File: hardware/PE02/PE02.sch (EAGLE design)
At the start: 23 parts, among them IC1 MSP430G2231, IC2 TPS78233

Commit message: Fixed buzzer, need to alter package of GND sewtab to make pad for vibration sensor
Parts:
- added JP1: (no value), adafruit:PINHD-1X1CB
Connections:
- net BUZZ: now also JP1.1
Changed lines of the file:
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@@
 <part name="TP1" library="adafruit" deviceset="SEWTAP" device="0.4IN"/>
 <part name="TP2" library="adafruit" deviceset="SEWTAP" device="0.4IN"/>
+<part name="JP1" library="adafruit" deviceset="PINHD-1X1" device="CB"/>
 </parts>
 <sheets>
@@
 <instance part="TP1" gate="G$1" x="-30.48" y="50.8" rot="R180"/>
 <instance part="TP2" gate="G$1" x="-30.48" y="35.56" rot="R180"/>
+<instance part="JP1" gate="G$1" x="86.36" y="73.66" rot="R270"/>
 </instances>
 <busses>
@@
 <segment>
 <pinref part="IC1" gate="G$1" pin="12"/>
-<wire x1="68.58" y1="60.96" x2="76.2" y2="60.96" width="0.1524" layer="91"/>
 <label x="71.12" y="60.96" size="1.778" layer="95"/>
-</segment>
-</net>
+<wire x1="86.36" y1="60.96" x2="68.58" y2="60.96" width="0.1524" layer="91"/>
+<pinref part="JP1" gate="G$1" pin="1"/>
+<wire x1="86.36" y1="60.96" x2="86.36" y2="76.2" width="0.1524" layer="91"/>
+</segment>
+</net>

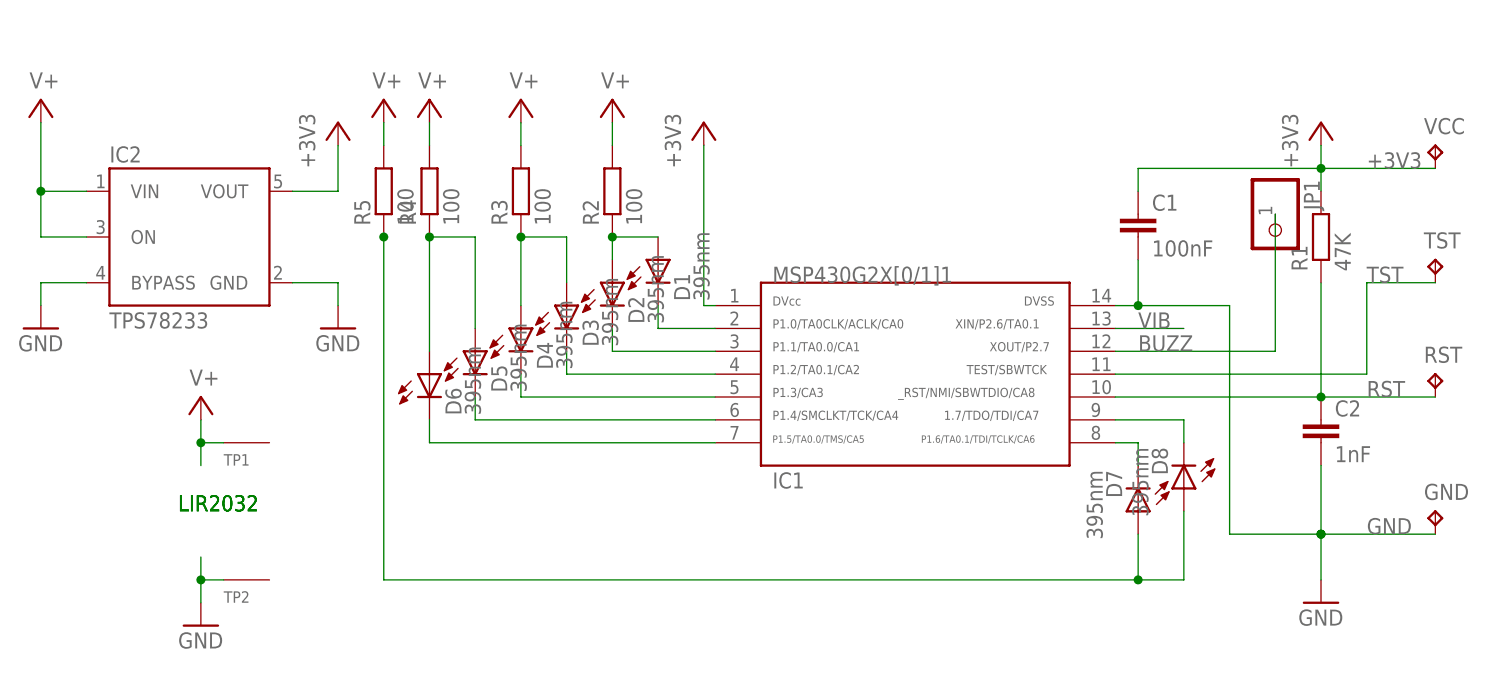
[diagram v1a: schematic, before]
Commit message: 2.2V supply, pullup vibration sensor to output pin
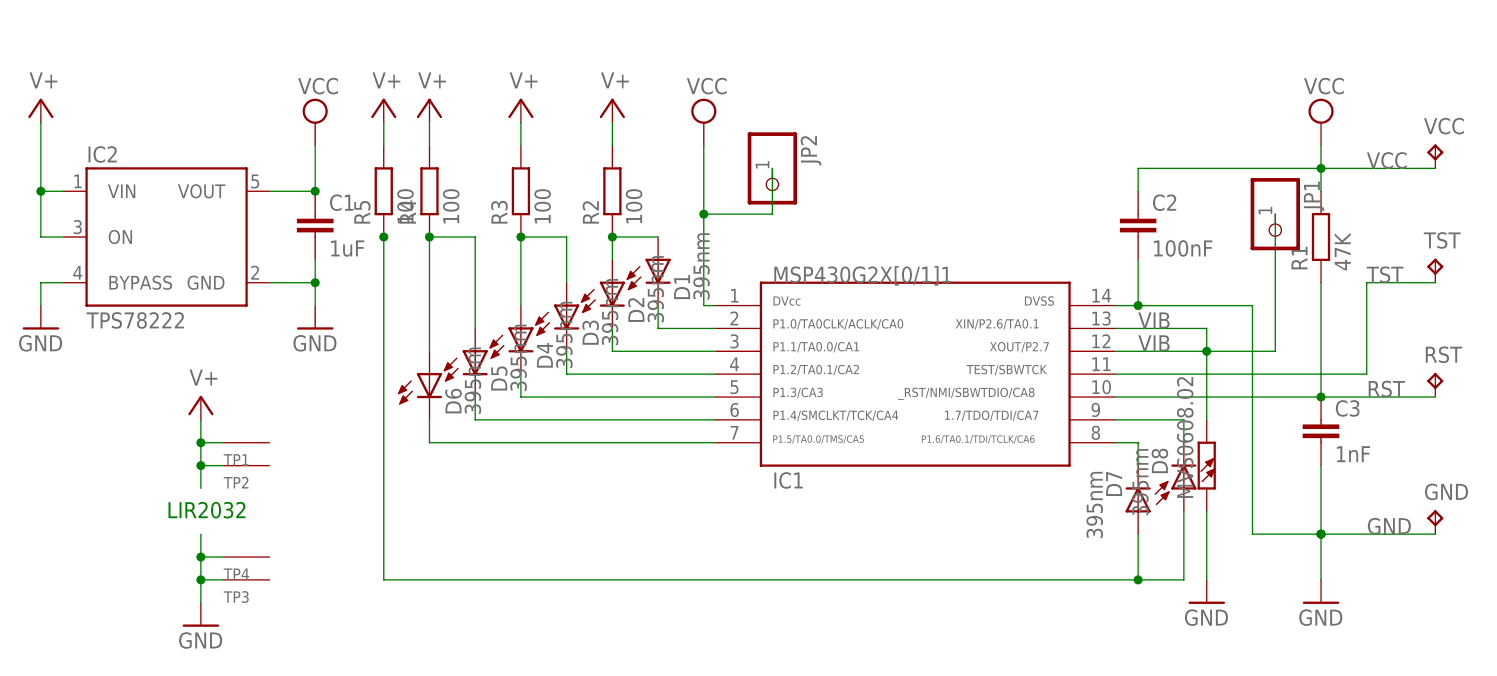
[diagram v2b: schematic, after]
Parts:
- added C3: 1nF, SparkFun:CAP0805
- added JP2: (no value), adafruit:PINHD-1X1CB
- added MVS0608.02: (no value), rcl:R-EU_R1210
- added TP3: SEWTAP0.4IN, adafruit:SEWTAP0.4IN
- added TP4: SEWTAB, t0mpr1c3:SEWTAB
- C1: value 100nF -> 1uF
- C2: value 1nF -> 100nF
- IC2: value TPS78233 -> TPS78222
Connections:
- removed net +3V3: C1.1, IC1.1, IC2.VOUT, R1.2, VCC.TP
- removed net BUZZ: IC1.12, JP1.1
- new net VCC: C1.1, C2.1, IC1.1, IC2.VOUT, JP2.1, R1.2, VCC.TP
- net GND: now also C3.2, MVS0608.02.1, TP3.SEW, TP4.SEW; no longer TP2.SEW
- net RST: now also C3.1; no longer C2.1
- net V+: now also TP2.SEW
- net VIB: now also IC1.12, JP1.1, MVS0608.02.2
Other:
- moved on the sheet: C1, C2, IC2, TP2

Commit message: moved buzzer output to P1.2
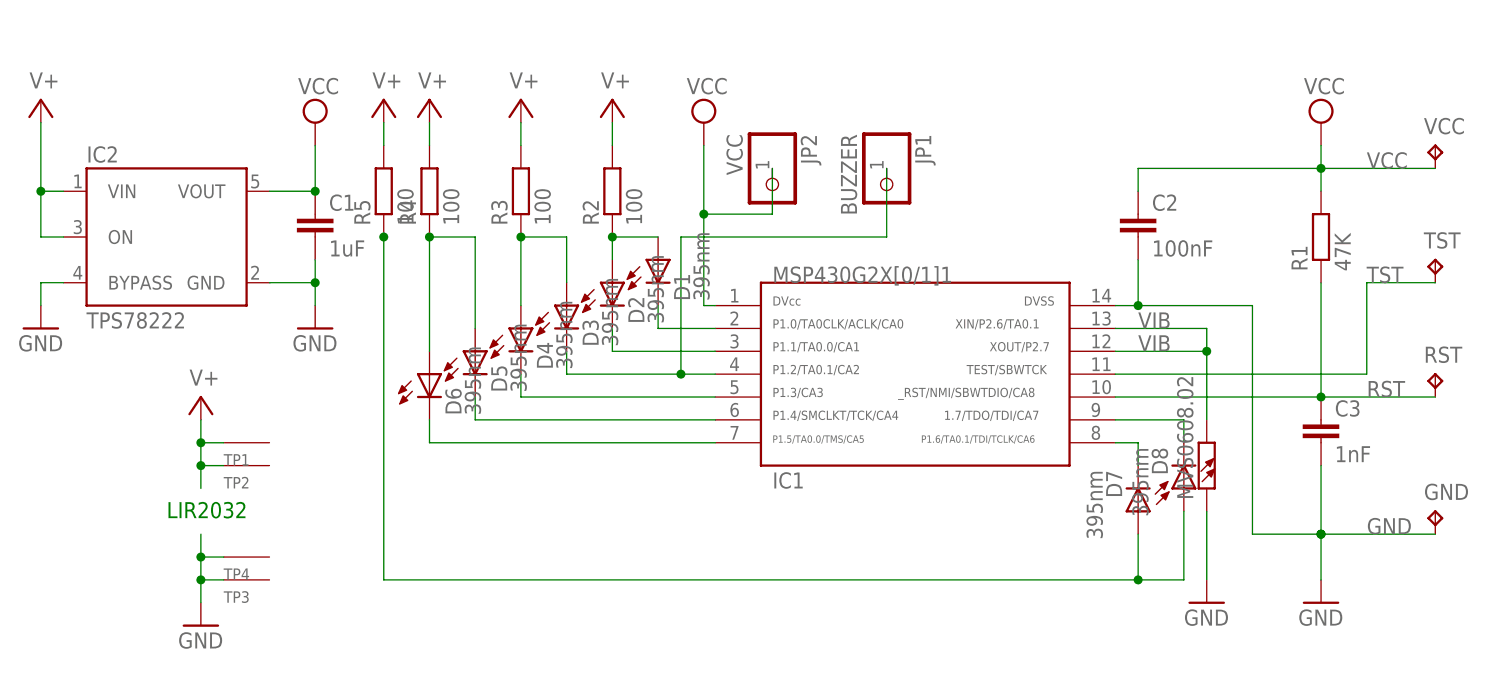
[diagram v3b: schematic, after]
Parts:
- JP1: value (none) -> BUZZER
- JP2: value (none) -> VCC
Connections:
- net N$6: now also JP1.1
- net VIB: no longer JP1.1
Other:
- moved on the sheet: JP1
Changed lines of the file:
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@@
 <part name="TP1" library="adafruit" deviceset="SEWTAP" device="0.4IN"/>
 <part name="TP2" library="adafruit" deviceset="SEWTAP" device="0.4IN"/>
-<part name="JP1" library="adafruit" deviceset="PINHD-1X1" device="CB"/>
+<part name="JP1" library="adafruit" deviceset="PINHD-1X1" device="CB" value="BUZZER"/>
 <part name="TP3" library="adafruit" deviceset="SEWTAP" device="0.4IN"/>
 <part name="TP4" library="t0mpr1c3" deviceset="SEWTAB" device=""/>
-<part name="JP2" library="adafruit" deviceset="PINHD-1X1" device="CB"/>
+<part name="JP2" library="adafruit" deviceset="PINHD-1X1" device="CB" value="VCC"/>
 <part name="MVS0608.02" library="rcl" deviceset="R-EU_" device="R1210"/>
 <part name="GND5" library="supply1" deviceset="GND" device=""/>
@@
 <instance part="TP1" gate="G$1" x="-30.48" y="50.8" rot="R180"/>
 <instance part="TP2" gate="G$1" x="-30.48" y="48.26" rot="R180"/>
-<instance part="JP1" gate="G$1" x="86.36" y="73.66" rot="R270"/>
+<instance part="JP1" gate="G$1" x="43.18" y="78.74" rot="R270"/>
 <instance part="TP3" gate="G$1" x="-30.48" y="35.56" rot="R180"/>
 <instance part="TP4" gate="G$1" x="-30.48" y="38.1" rot="R180"/>
@@
 <label x="71.12" y="60.96" size="1.778" layer="95"/>
 <wire x1="78.74" y1="60.96" x2="78.74" y2="63.5" width="0.1524" layer="91"/>
-<wire x1="86.36" y1="60.96" x2="78.74" y2="60.96" width="0.1524" layer="91"/>
-<pinref part="JP1" gate="G$1" pin="1"/>
 <wire x1="78.74" y1="60.96" x2="68.58" y2="60.96" width="0.1524" layer="91"/>
-<wire x1="86.36" y1="60.96" x2="86.36" y2="76.2" width="0.1524" layer="91"/>
 <junction x="78.74" y="60.96"/>
 </segment>
@@
 <pinref part="IC1" gate="G$1" pin="4"/>
 <pinref part="D3" gate="LED" pin="C"/>
-<wire x1="24.13" y1="58.42" x2="7.62" y2="58.42" width="0.1524" layer="91"/>
+<wire x1="24.13" y1="58.42" x2="20.32" y2="58.42" width="0.1524" layer="91"/>
+<wire x1="20.32" y1="58.42" x2="7.62" y2="58.42" width="0.1524" layer="91"/>
 <wire x1="7.62" y1="58.42" x2="7.62" y2="60.96" width="0.1524" layer="91"/>
-</segment>
-</net>
-<net name="N$7" class="0">
-<segment>
-<pinref part="IC1" gate="G$1" pin="3"/>
-<wire x1="24.13" y1="60.96" x2="12.7" y2="60.96" width="0.1524" layer="91"/>
-<pinref part="D2" gate="LED" pin="C"/>
-<wire x1="12.7" y1="60.96" x2="12.7" y2="63.5" width="0.1524" layer="91"/>
+<junction x="20.32" y="58.42"/>
+<pinref part="JP1" gate="G$1" pin="1"/>
+<wire x1="43.18" y1="81.28" x2="43.18" y2="73.66" width="0.1524" layer="91"/>
+<wire x1="43.18" y1="73.66" x2="20.32" y2="73.66" width="0.1524" layer="91"/>
+<wire x1="20.32" y1="58.42" x2="20.32" y2="73.66" width="0.1524" layer="91"/>
 </segment>
 </net>
@@
 </segment>
 </net>
+<net name="N$12" class="0">
+<segment>
+<pinref part="D2" gate="LED" pin="C"/>
+<pinref part="IC1" gate="G$1" pin="3"/>
+<wire x1="24.13" y1="60.96" x2="12.7" y2="60.96" width="0.1524" layer="91"/>
+<wire x1="12.7" y1="60.96" x2="12.7" y2="63.5" width="0.1524" layer="91"/>
+</segment>
+</net>

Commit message: Added Molex Pico-EZmate connector, removed bottom sewtab
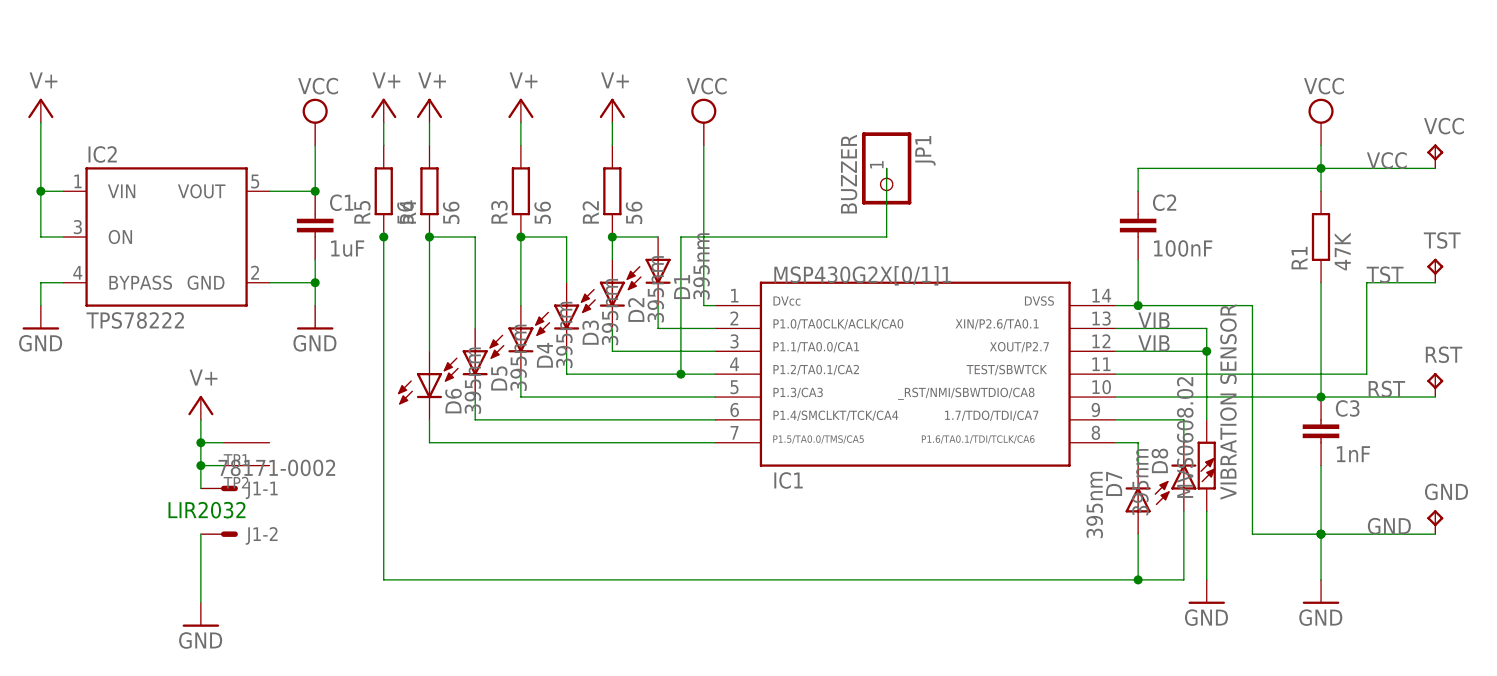
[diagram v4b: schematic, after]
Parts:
- removed JP2: VCC, adafruit:PINHD-1X1CB
- removed TP3: SEWTAP0.4IN, adafruit:SEWTAP0.4IN
- removed TP4: SEWTAB, t0mpr1c3:SEWTAB
- added J1: 78171-0002, con-molex-pico-ezmate:78171-0002
- MVS0608.02: value (none) -> VIBRATION SENSOR
- R2, R3, R4, R5: value 100 -> 56
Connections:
- net GND: now also J1-2.S; no longer TP3.SEW, TP4.SEW
- net V+: now also J1-1.S
- net VCC: no longer JP2.1
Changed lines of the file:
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@@
 <part name="+3V3" library="supply2" deviceset="VCC" device=""/>
 <part name="GND4" library="supply1" deviceset="GND" device=""/>
-<part name="R2" library="rcl" deviceset="R-EU_" device="R0603" value="100"/>
-<part name="R5" library="rcl" deviceset="R-EU_" device="R0603" value="100"/>
+<part name="R2" library="rcl" deviceset="R-EU_" device="R0603" value="56"/>
+<part name="R5" library="rcl" deviceset="R-EU_" device="R0603" value="56"/>
 <part name="SUPPLY4" library="supply2" deviceset="V+" device=""/>
-<part name="R4" library="rcl" deviceset="R-EU_" device="R0603" value="100"/>
+<part name="R4" library="rcl" deviceset="R-EU_" device="R0603" value="56"/>
 <part name="SUPPLY5" library="supply2" deviceset="V+" device=""/>
-<part name="R3" library="rcl" deviceset="R-EU_" device="R0603" value="100"/>
+<part name="R3" library="rcl" deviceset="R-EU_" device="R0603" value="56"/>
 <part name="SUPPLY6" library="supply2" deviceset="V+" device=""/>
 <part name="VCC" library="testpad" deviceset="TP" device="TP10R" value="TPTP10R"/>
@@
 <part name="TP2" library="adafruit" deviceset="SEWTAP" device="0.4IN"/>
 <part name="JP1" library="adafruit" deviceset="PINHD-1X1" device="CB" value="BUZZER"/>
-<part name="TP3" library="adafruit" deviceset="SEWTAP" device="0.4IN"/>
-<part name="TP4" library="t0mpr1c3" deviceset="SEWTAB" device=""/>
-<part name="JP2" library="adafruit" deviceset="PINHD-1X1" device="CB" value="VCC"/>
-<part name="MVS0608.02" library="rcl" deviceset="R-EU_" device="R1210"/>
+<part name="MVS0608.02" library="rcl" deviceset="R-EU_" device="R1210" value="VIBRATION SENSOR"/>
 <part name="GND5" library="supply1" deviceset="GND" device=""/>
 <part name="C1" library="SparkFun" deviceset="CAP" device="0805" value="1uF"/>
+<part name="J1" library="con-molex-pico-ezmate" deviceset="78171-0002" device=""/>
 </parts>
 <sheets>
@@
 <instance part="TP2" gate="G$1" x="-30.48" y="48.26" rot="R180"/>
 <instance part="JP1" gate="G$1" x="43.18" y="78.74" rot="R270"/>
-<instance part="TP3" gate="G$1" x="-30.48" y="35.56" rot="R180"/>
-<instance part="TP4" gate="G$1" x="-30.48" y="38.1" rot="R180"/>
-<instance part="JP2" gate="G$1" x="30.48" y="78.74" rot="R270"/>
 <instance part="MVS0608.02" gate="G$1" x="78.74" y="48.26" rot="R90"/>
 <instance part="GND5" gate="1" x="78.74" y="33.02"/>
 <instance part="C1" gate="G$1" x="-20.32" y="73.66"/>
+<instance part="J1" gate="-1" x="-30.48" y="45.72"/>
+<instance part="J1" gate="-2" x="-30.48" y="40.64"/>
 </instances>
 <busses>
@@
 </segment>
 <segment>
-<pinref part="GND3" gate="1" pin="GND"/>
-<wire x1="-33.02" y1="38.1" x2="-33.02" y2="35.56" width="0.1524" layer="91"/>
-<junction x="-33.02" y="35.56"/>
-<wire x1="-33.02" y1="35.56" x2="-33.02" y2="33.02" width="0.1524" layer="91"/>
-<pinref part="TP3" gate="G$1" pin="SEW"/>
-<wire x1="-30.48" y1="35.56" x2="-33.02" y2="35.56" width="0.1524" layer="91"/>
-<pinref part="TP4" gate="G$1" pin="SEW"/>
-<wire x1="-30.48" y1="38.1" x2="-33.02" y2="38.1" width="0.1524" layer="91"/>
-<wire x1="-33.02" y1="38.1" x2="-33.02" y2="40.64" width="0.1524" layer="91"/>
-<junction x="-33.02" y="38.1"/>
-</segment>
-<segment>
 <pinref part="IC2" gate="A" pin="GND"/>
 <pinref part="GND1" gate="1" pin="GND"/>
@@
 <pinref part="MVS0608.02" gate="G$1" pin="1"/>
 <wire x1="78.74" y1="35.56" x2="78.74" y2="43.18" width="0.1524" layer="91"/>
+</segment>
+<segment>
+<pinref part="GND3" gate="1" pin="GND"/>
+<wire x1="-33.02" y1="40.64" x2="-33.02" y2="33.02" width="0.1524" layer="91"/>
+<pinref part="J1" gate="-2" pin="S"/>
 </segment>
 </net>
@@
 <wire x1="24.13" y1="66.04" x2="22.86" y2="66.04" width="0.1524" layer="91"/>
 <pinref part="+3V2" gate="G$1" pin="VCC"/>
-<wire x1="22.86" y1="83.82" x2="22.86" y2="76.2" width="0.1524" layer="91"/>
-<wire x1="22.86" y1="76.2" x2="22.86" y2="66.04" width="0.1524" layer="91"/>
-<wire x1="30.48" y1="81.28" x2="30.48" y2="76.2" width="0.1524" layer="91"/>
-<wire x1="30.48" y1="76.2" x2="22.86" y2="76.2" width="0.1524" layer="91"/>
-<junction x="22.86" y="76.2"/>
-<pinref part="JP2" gate="G$1" pin="1"/>
+<wire x1="22.86" y1="83.82" x2="22.86" y2="66.04" width="0.1524" layer="91"/>
 </segment>
 <segment>
@@
 <wire x1="-30.48" y1="50.8" x2="-33.02" y2="50.8" width="0.1524" layer="91"/>
 <pinref part="TP1" gate="G$1" pin="SEW"/>
-<junction x="-33.02" y="48.26"/>
-<wire x1="-33.02" y1="48.26" x2="-33.02" y2="45.72" width="0.1524" layer="91"/>
 <pinref part="TP2" gate="G$1" pin="SEW"/>
 <wire x1="-30.48" y1="48.26" x2="-33.02" y2="48.26" width="0.1524" layer="91"/>
-</segment>
-<segment>
+<wire x1="-33.02" y1="45.72" x2="-33.02" y2="48.26" width="0.1524" layer="91"/>
+<junction x="-33.02" y="48.26"/>
+<pinref part="J1" gate="-1" pin="S"/>
+</segment>
+<segment>
